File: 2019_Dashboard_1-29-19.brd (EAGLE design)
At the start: 93.7 x 49.2 mm, 55 parts, among them IC1 MCP23017SO, Q1 TN0602N3, Q2 TN0602N3, Q3 TN0602N3, Q4 TN0602N3, Q5 TN0602N3, U1 TLC59281, Y1 16MHz

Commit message: Add files via upload
Finished?
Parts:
- added C10: 100pF, SparkFun-Capacitors:0603
- added C11: 1.0uF, SparkFun-Capacitors:0805
- added C7: 10uF, SparkFun-Capacitors:0805
- added C8: 10nF, SparkFun-Capacitors:0603
- added C9: 22uF, SparkFun-Capacitors:0805
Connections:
- net GND: now also C10.2, C11.2, C7.2, C8.2, C9.2
- net VCC: now also C10.1, C11.1, C7.1, C8.1, C9.1
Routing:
- net GND: track 221.4 -> 229.7 mm, vias 7 -> 12
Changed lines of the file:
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@@
 </element>
 <element name="R24" library="resistor" library_urn="urn:adsk.eagle:library:348" package="R0603" package3d_urn="urn:adsk.eagle:package:26057/1" value="2.52k" x="111.76" y="53.34" rot="MR270"/>
+<element name="C7" library="SparkFun-Capacitors" library_urn="urn:adsk.eagle:library:510" package="0805" package3d_urn="urn:adsk.eagle:package:37429/1" value="10uF" x="121.92" y="67.31" rot="R180">
+<attribute name="PROD_ID" value="CAP-11330" x="121.92" y="67.31" size="1.778" layer="27" rot="R180" display="off"/>
+</element>
+<element name="C8" library="SparkFun-Capacitors" library_urn="urn:adsk.eagle:library:510" package="0603" package3d_urn="urn:adsk.eagle:package:37414/1" value="10nF" x="128.27" y="67.31" rot="R180">
+<attribute name="PROD_ID" value="CAP-00867" x="128.27" y="67.31" size="1.778" layer="27" rot="R180" display="off"/>
+</element>
+<element name="C9" library="SparkFun-Capacitors" library_urn="urn:adsk.eagle:library:510" package="0805" package3d_urn="urn:adsk.eagle:package:37429/1" value="22uF" x="134.62" y="67.31" rot="R180">
+<attribute name="PROD_ID" value="CAP-08402" x="134.62" y="67.31" size="1.778" layer="27" rot="R180" display="off"/>
+</element>
+<element name="C10" library="SparkFun-Capacitors" library_urn="urn:adsk.eagle:library:510" package="0603" package3d_urn="urn:adsk.eagle:package:37414/1" value="100pF" x="134.62" y="62.23" rot="R180">
+<attribute name="PROD_ID" value="CAP-07883" x="134.62" y="62.23" size="1.778" layer="27" rot="R180" display="off"/>
+</element>
+<element name="C11" library="SparkFun-Capacitors" library_urn="urn:adsk.eagle:library:510" package="0805" package3d_urn="urn:adsk.eagle:package:37429/1" value="1.0uF" x="128.27" y="62.23" rot="R180">
+<attribute name="PROD_ID" value="CAP-11625" x="128.27" y="62.23" size="1.778" layer="27" rot="R180" display="off"/>
+</element>
 </elements>
 <signals>
@@
 <vertex x="139.7" y="78.74"/>
 </polygon>
+<contactref element="C10" pad="2"/>
+<contactref element="C9" pad="2"/>
+<contactref element="C8" pad="2"/>
+<contactref element="C7" pad="2"/>
+<contactref element="C11" pad="2"/>
+<via x="119.38" y="67.31" extent="1-16" drill="0.35"/>
+<via x="125.73" y="67.31" extent="1-16" drill="0.35"/>
+<via x="132.08" y="67.31" extent="1-16" drill="0.35"/>
+<via x="125.73" y="62.23" extent="1-16" drill="0.35"/>
+<via x="132.08" y="62.23" extent="1-16" drill="0.35"/>
+<wire x1="121.02" y1="67.31" x2="119.38" y2="67.31" width="0.4064" layer="1"/>
+<wire x1="127.42" y1="67.31" x2="125.73" y2="67.31" width="0.4064" layer="1"/>
+<wire x1="127.37" y1="62.23" x2="125.73" y2="62.23" width="0.4064" layer="1"/>
+<wire x1="133.77" y1="62.23" x2="132.08" y2="62.23" width="0.4064" layer="1"/>
+<wire x1="133.72" y1="67.31" x2="132.08" y2="67.31" width="0.4064" layer="1"/>
 <wire x1="82.57" y1="65.36" x2="82.5756" y2="65.96849375" width="0" layer="19" extent="16-16"/>
 </signal>
@@
 <vertex x="139.7" y="78.74"/>
 </polygon>
+<contactref element="C7" pad="1"/>
+<contactref element="C11" pad="1"/>
+<contactref element="C8" pad="1"/>
+<contactref element="C9" pad="1"/>
+<contactref element="C10" pad="1"/>
 </signal>
 <signal name="OSC1">

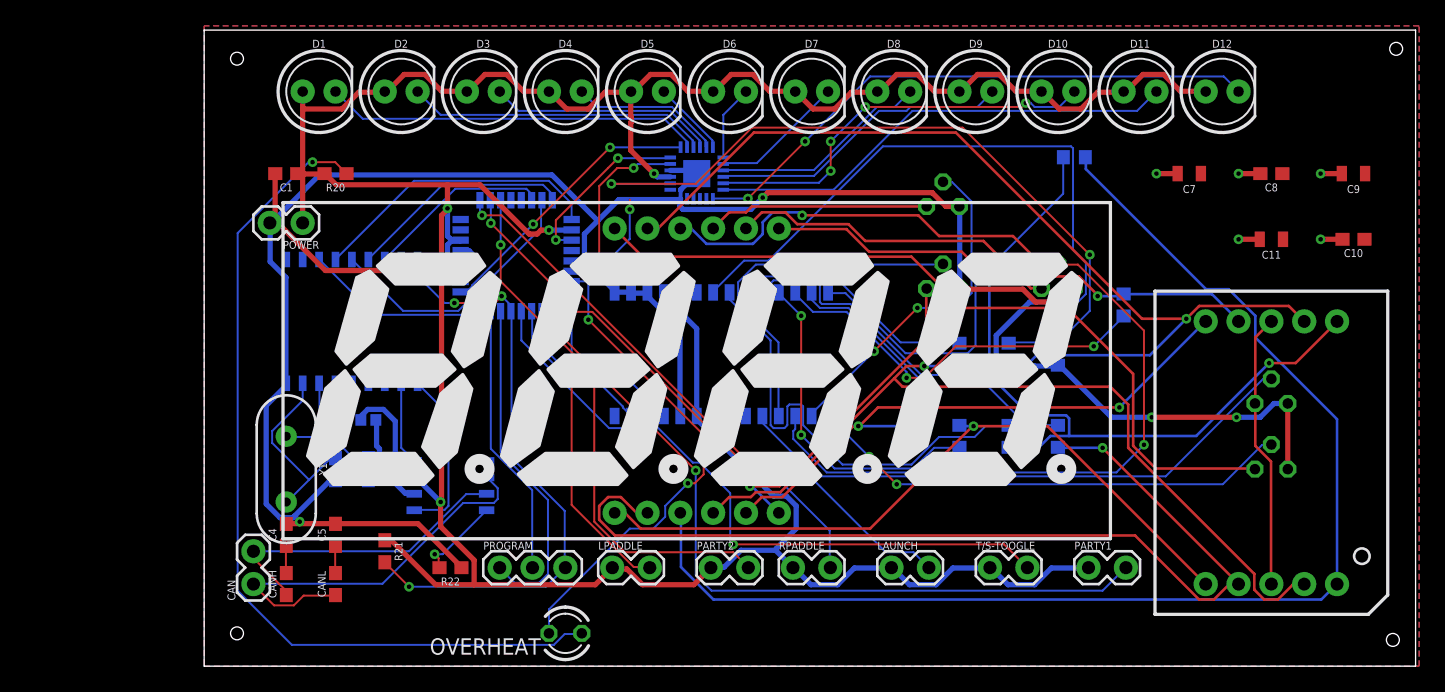
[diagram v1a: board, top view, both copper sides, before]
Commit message: Added correct footprint for gear position display
Committing before I actually wire it up
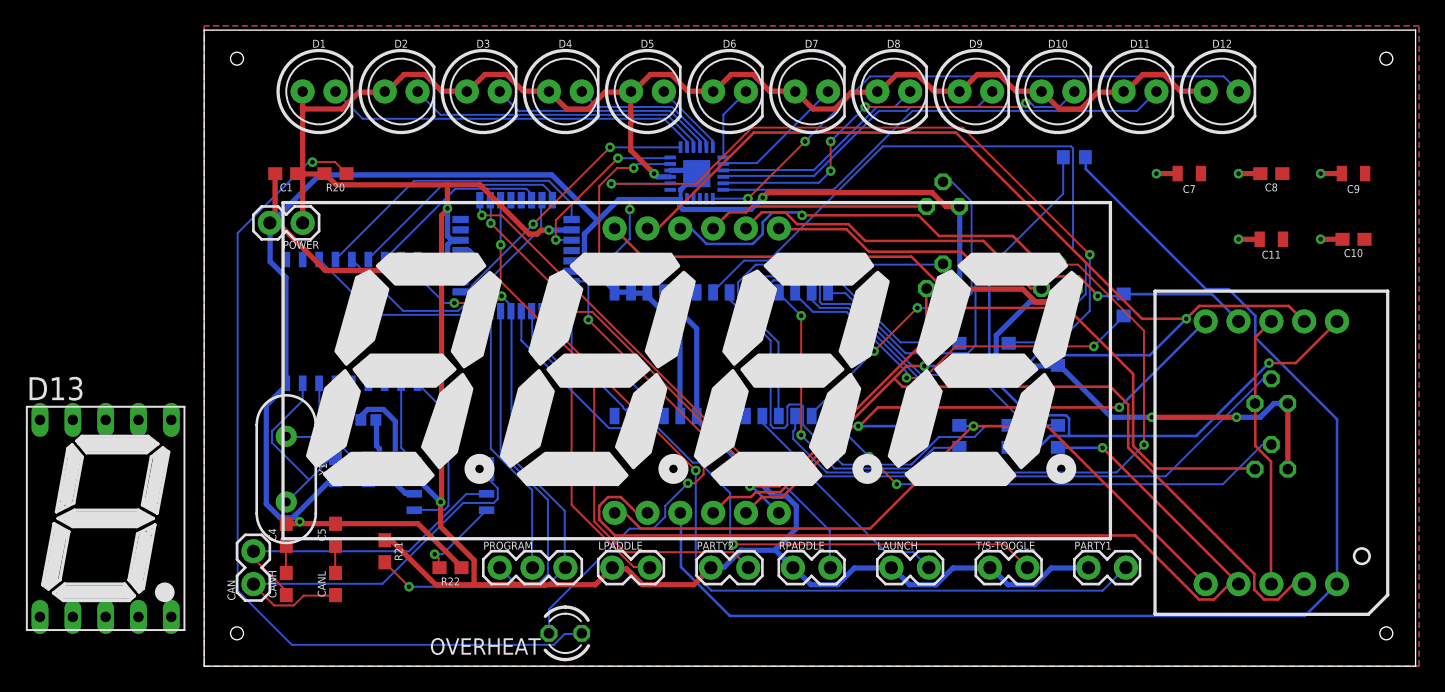
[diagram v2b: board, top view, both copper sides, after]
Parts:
- added D13: (no value), special:7SEG-13
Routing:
- net N$10: track 98.7 -> 99.7 mm
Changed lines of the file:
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@@
 <?xml version="1.0" encoding="utf-8"?>
 <!DOCTYPE eagle SYSTEM "eagle.dtd">
-<eagle version="9.1.3">
+<eagle version="9.1.0">
 <drawing>
 <settings>
@@
 <setting verticaltext="up"/>
 </settings>
-<grid distance="50" unitdist="mil" unit="mil" style="lines" multiple="1" display="no" altdistance="5" altunitdist="mil" altunit="mil"/>
+<grid distance="50" unitdist="mil" unit="mil" style="lines" multiple="1" display="yes" altdistance="5" altunitdist="mil" altunit="mil"/>
 <layers>
 <layer number="1" name="Top" color="4" fill="1" visible="yes" active="yes"/>
@@
 <wire x1="139.426" y1="78.41" x2="45.72" y2="78.41" width="0" layer="20"/>
 <wire x1="45.72" y1="78.41" x2="45.72" y2="29.21" width="0" layer="20"/>
-<hole x="137.922" y="76.962" drill="1"/>
+<hole x="137.16" y="76.2" drill="1"/>
 <hole x="48.26" y="31.75" drill="1"/>
 <hole x="48.26" y="76.2" drill="1"/>
-<hole x="137.668" y="31.242" drill="1"/>
+<hole x="137.16" y="31.75" drill="1"/>
+<dimension x1="109.22" y1="60.96" x2="107.95" y2="43.18" x3="114.722259375" y3="51.631621875" textsize="1.778" layer="1"/>
+<dimension x1="130.81" y1="38.1" x2="130.81" y2="53.34" x3="132.08" y3="45.72" textsize="1.778" layer="1"/>
+<dimension x1="135.89" y1="58.42" x2="134.62" y2="33.02" x3="144.566221875" y3="45.2544375" textsize="1.778" layer="1"/>
+<dimension x1="123.2154" y1="58.3692" x2="113.919" y2="67.6656" x3="101.4349" y3="45.8851" textsize="1.778" layer="1"/>
+<dimension x1="133.35" y1="55.88" x2="133.35" y2="35.56" x3="135.89" y3="45.72" textsize="1.778" layer="1"/>
+<dimension x1="123.19" y1="55.88" x2="133.35" y2="55.88" x3="128.27" y3="59.69" textsize="1.778" layer="1"/>
+<dimension x1="33.02" y1="33.02" x2="43.18" y2="33.02" x3="38.1" y3="27.94" textsize="1.778" layer="1"/>
+<dimension x1="33.02" y1="33.02" x2="33.02" y2="48.26" x3="29.21" y3="40.64" textsize="1.778" layer="1"/>
 </plain>
 <attributes>
@@
 <attribute name="PROD_ID" value="CAP-11625" x="128.27" y="62.23" size="1.778" layer="27" rot="R180" display="off"/>
 </element>
+<element name="D13" library="special" library_urn="urn:adsk.eagle:library:367" package="7SEG-13" package3d_urn="urn:adsk.eagle:package:26668/2" value="" x="38.1" y="40.64"/>
 </elements>
 <signals>
@@
 <wire x1="113.919" y1="68.58" x2="113.88" y2="68.58" width="0.2032" layer="16"/>
 <wire x1="82.6008" y1="36.8808" x2="82.6008" y2="41.0718" width="0.2032" layer="16"/>
-<wire x1="85.1154" y1="34.3662" x2="82.6008" y2="36.8808" width="0.2032" layer="16"/>
-<wire x1="132.1308" y1="34.3662" x2="85.1154" y2="34.3662" width="0.2032" layer="16"/>
-<wire x1="133.2738" y1="35.5092" x2="132.1308" y2="34.3662" width="0.2032" layer="16"/>
+<wire x1="86.3854" y1="33.0962" x2="82.6008" y2="36.8808" width="0.2032" layer="16"/>
+<wire x1="130.8608" y1="33.0962" x2="86.3854" y2="33.0962" width="0.2032" layer="16"/>
+<wire x1="133.2738" y1="35.5092" x2="130.8608" y2="33.0962" width="0.2032" layer="16"/>
 <wire x1="82.6008" y1="41.0718" x2="82.55" y2="41.0718" width="0.2032" layer="16"/>
 <wire x1="133.2738" y1="35.5092" x2="133.35" y2="35.56" width="0.2032" layer="16"/>
